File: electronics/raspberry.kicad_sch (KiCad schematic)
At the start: 13 parts, among them J1 Raspberry_Pi_4, J2 TUB00154 Analog Control, U1 LT1009CZ, U2 TLV5618A, U3 SFH900, U4 SFH900, U5 MCP3202, U7 LM4040LP-5

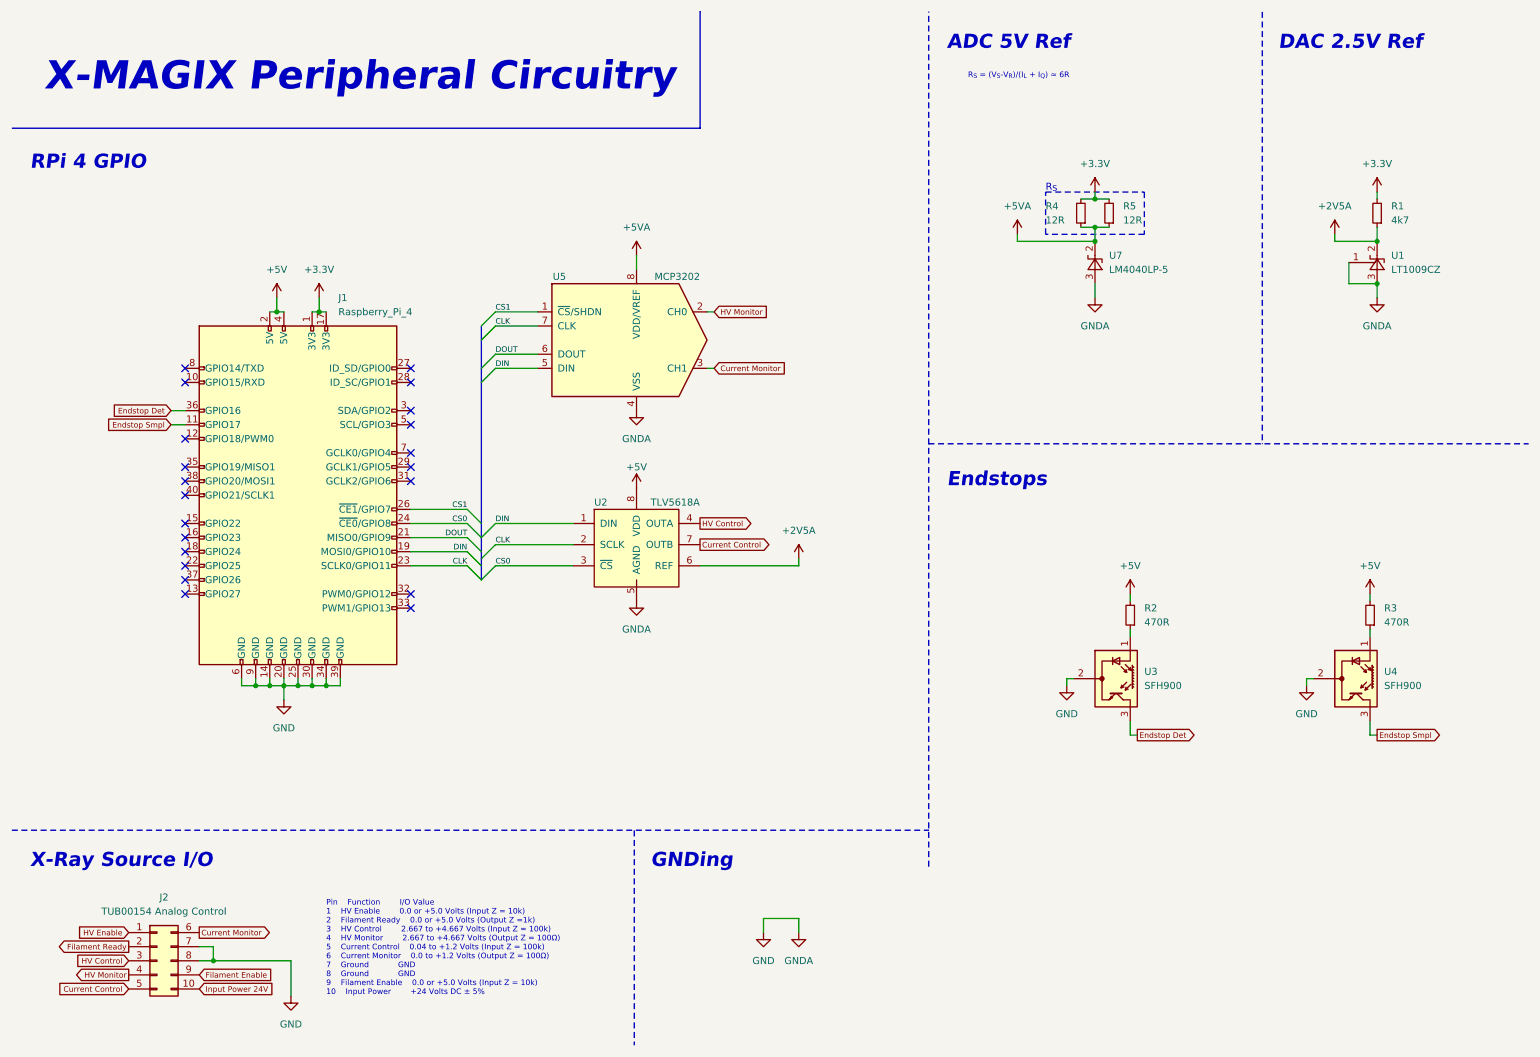
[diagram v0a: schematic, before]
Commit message: Tube Interface Board Docs
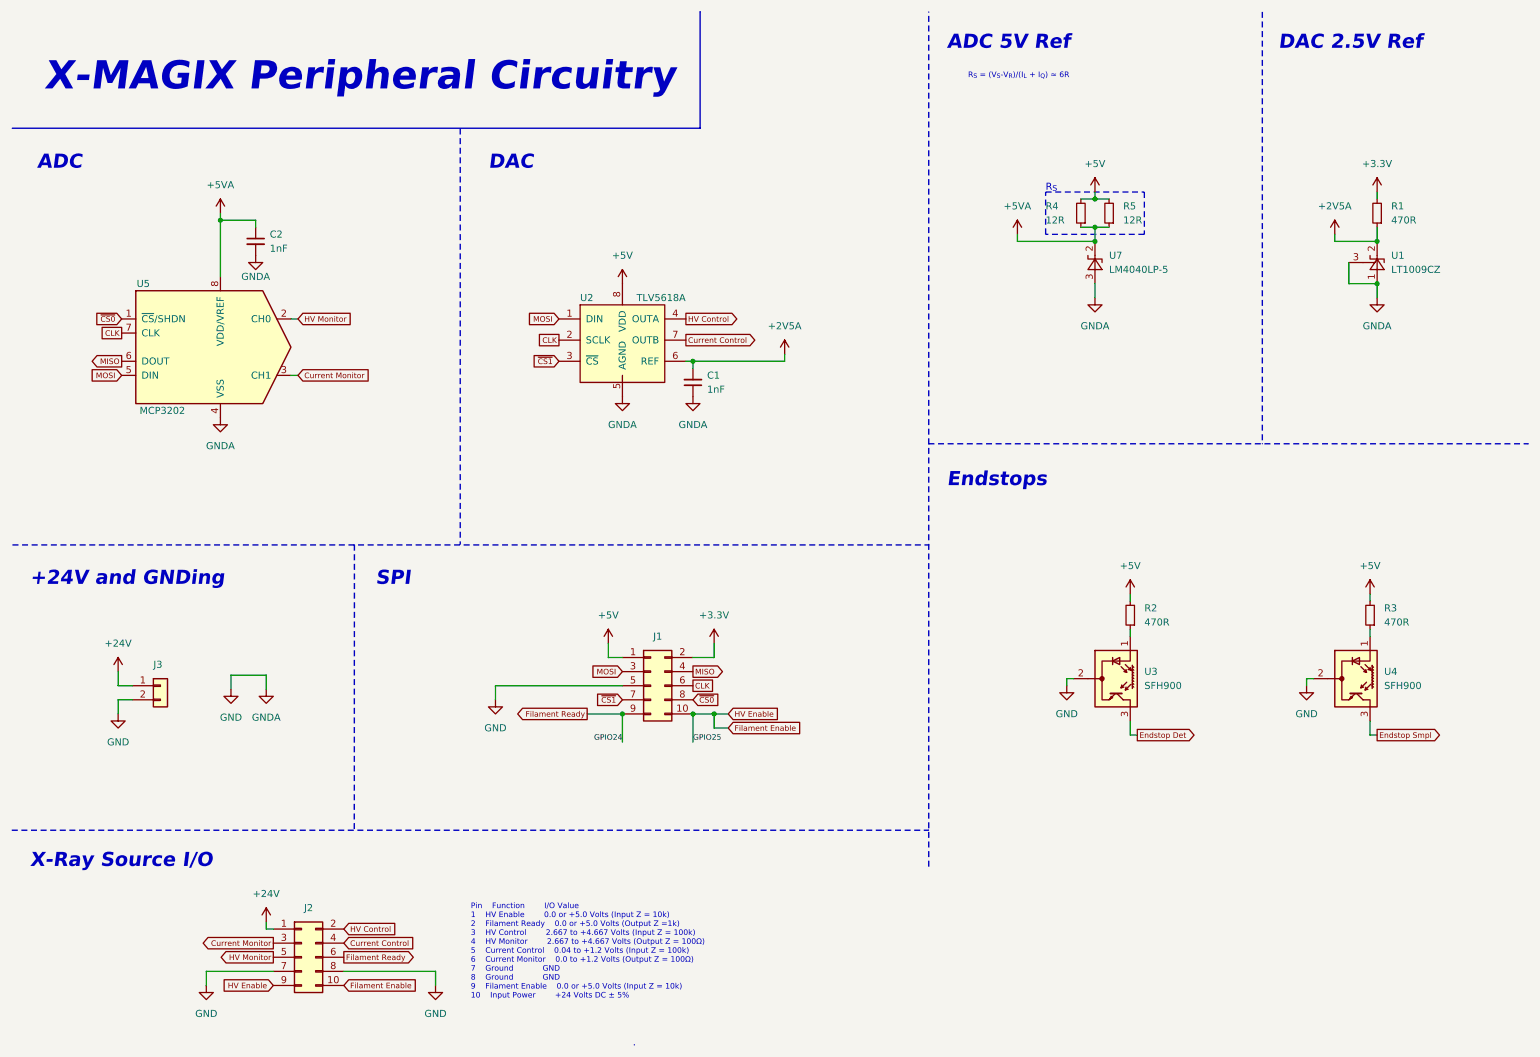
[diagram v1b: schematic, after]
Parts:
- removed J1: Raspberry_Pi_4, symbol Connector:Raspberry_Pi_2_3
- removed J2: TUB00154 Analog Control, symbol Connector_Generic:Conn_02x05_Top_Bottom
- added C1, C2: 1nF, custom_footprints:C_Disc_D3.0mm_W2.0mm_P2.54mm, symbol Device:C_Small
- added J1, J2: Conn_02x05_Counter_Clockwise, Connector_PinHeader_2.54mm:PinHeader_2x05_P2.54mm_Vertical, symbol Connector_Generic:Conn_02x05_Odd_Even
- added J3: Conn_01x02, custom_footprints:JST_XH_B2B-XH-A_1x02_P2.54mm_Vertical, symbol Connector_Generic:Conn_01x02
- R1: value 4k7 -> 470R; footprint (none) -> Resistor_THT:R_Axial_DIN0204_L3.6mm_D1.6mm_P7.62mm_Horizontal
- R4, R5: footprint (none) -> Resistor_THT:R_Axial_DIN0204_L3.6mm_D1.6mm_P7.62mm_Horizontal
- U1, U7: footprint Package_TO_SOT_THT:TO-92_Inline -> custom_footprints:TO-92L_Wide
- U2: footprint Package_SO:SOIC-8_3.9x4.9mm_P1.27mm -> Package_DIP:DIP-8_W7.62mm
- U5: footprint (none) -> Package_DIP:DIP-8_W7.62mm
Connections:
- net +2V5A: now also C1.2
- net +3.3V: now also J1.2 (Pin_2); no longer R4.2, R5.2
- net +5V: now also R4.2, R5.2, J1.1 (Pin_1)
- net +5VA: now also C2.1
- net CLK: now also J1.6 (Pin_6)
- net Current Control: now also J2.4 (Pin_4)
- net Current Monitor: now also J2.3 (Pin_3)
- net Filament Enable: now also J1.10 (Pin_10), J2.10 (Pin_10), J2.9 (Pin_9)
- net Filament Ready: now also J1.9 (Pin_9), J2.6 (Pin_6)
- net GND: now also C1.1, C2.2, J1.5 (Pin_5), J2.7 (Pin_7), J2.8 (Pin_8), J3.2 (Pin_2)
- net HV Control: now also J2.2 (Pin_2)
- net HV Monitor: now also J2.5 (Pin_5)
- net CS0 renamed ~{CS1}
- net ~{CS1}: now also J1.7 (Pin_7)
- net CS1 renamed ~{CS0}
- net ~{CS0}: now also J1.8 (Pin_8)
- net DIN renamed MOSI
- net MOSI: now also J1.3 (Pin_3)
- net DOUT renamed MISO
- net MISO: now also J1.4 (Pin_4)
- new net +24V: J2.1 (Pin_1), J3.1 (Pin_1)
- no-connect marks 21 -> 0
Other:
- note added: "+24V and GNDing"
- note added: "ADC"
- note added: "DAC"
- note added: "SPI"
- note removed: "GNDing"
- note removed: "RPi 4 GPIO"
- moved on the sheet: U2, U5

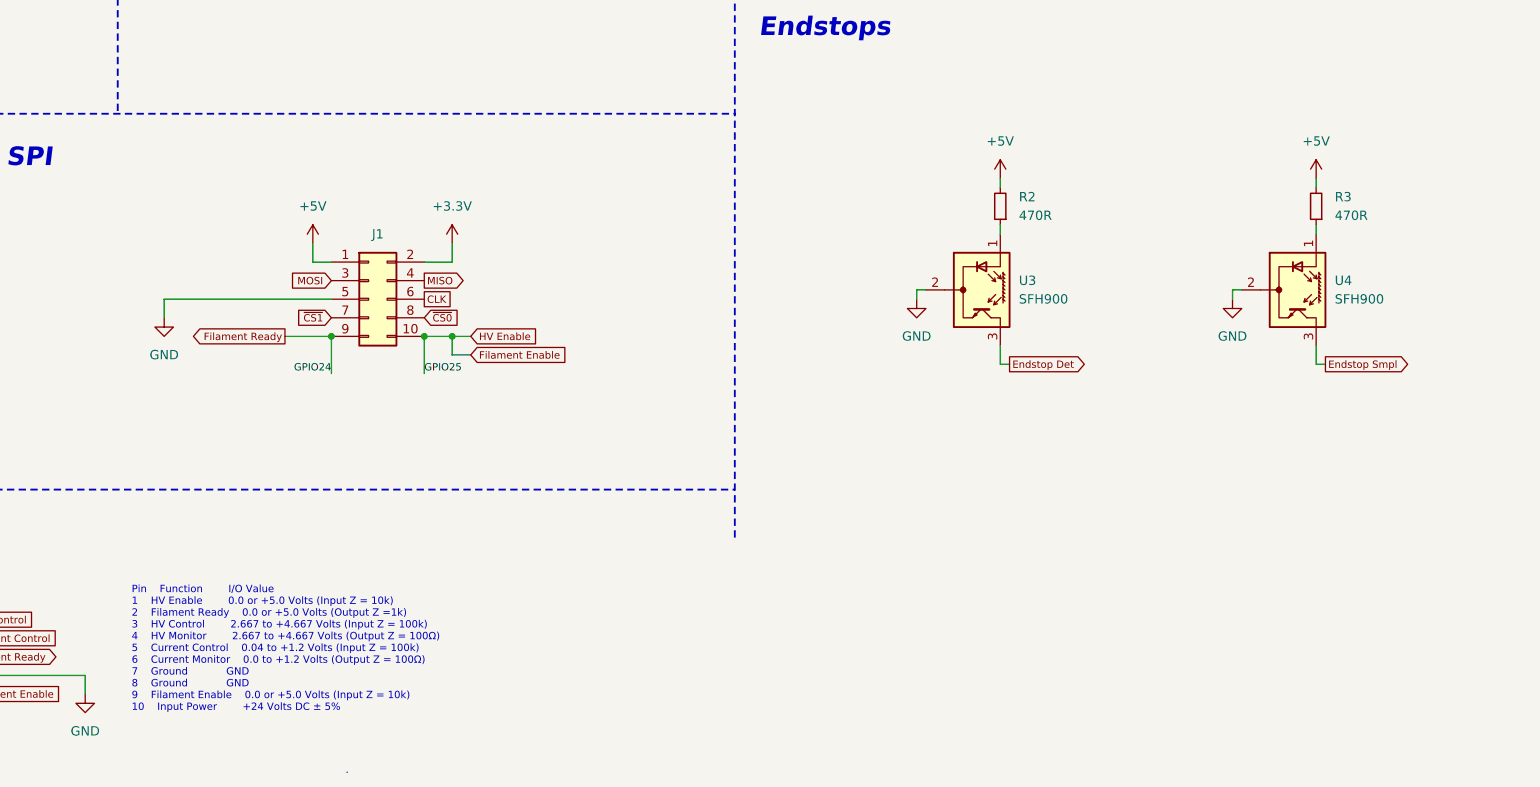
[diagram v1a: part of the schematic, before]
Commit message: endstops optical to tactile
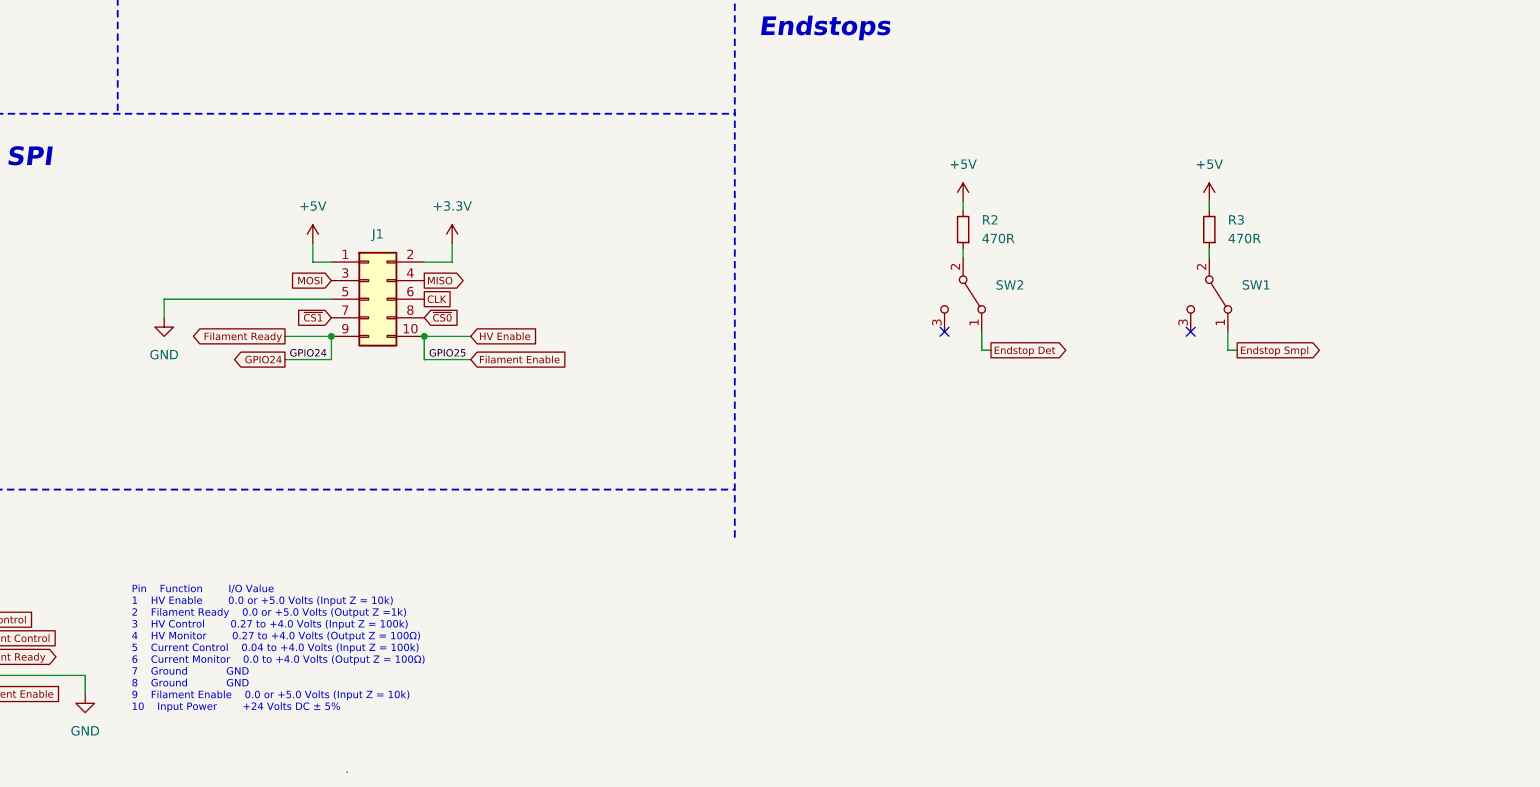
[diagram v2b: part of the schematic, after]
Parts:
- removed U3, U4: SFH900, OptoDevice:Siemens_SFH900, symbol Sensor_Proximity:SFH900
- added SW1, SW2: SW_SPDT, symbol Switch:SW_SPDT
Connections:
- net Endstop Det: now also SW2.1 (A)
- net Endstop Smpl: now also SW1.1 (A)
- net at R2.1: now also SW2.2 (B)
- net at R3.1: now also SW1.2 (B)
- no-connect marks 0 -> 2
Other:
- note added: "Pin Function I/O Value 1 HV Enable 0.0 or +5.0 Volts (Input Z = 10k) 2 Filament Ready 0.0 or +5.0 Volts (Output Z =1k) 3 HV Control 0.27 to +4.0 Volts (Input Z = 100k) 4 HV Monitor 0.27 to +4.0 Volts (Output Z = 100Ω) 5 Current Control 0.04 to +4.0 Volts (Input Z = 100k) 6 Current Monitor 0.0 to +4.0 Volts (Output Z = 100Ω) 7 Ground GND 8 Ground GND 9 Filament Enable 0.0 or +5.0 Volts (Input Z = 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"
- note removed: "Pin Function I/O Value 1 HV Enable 0.0 or +5.0 Volts (Input Z = 10k) 2 Filament Ready 0.0 or +5.0 Volts (Output Z =1k) 3 HV Control 2.667 to +4.667 Volts (Input Z = 100k) 4 HV Monitor 2.667 to +4.667 Volts (Output Z = 100Ω) 5 Current Control 0.04 to +1.2 Volts (Input Z = 100k) 6 Current Monitor 0.0 to +1.2 Volts (Output Z = 100Ω) 7 Ground GND 8 Ground GND 9 Filament Enable 0.0 or +5.0 Volts (Inpu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"
- company: Hochschule RheinMain -> RheinMain University of Applied Sciences
- moved on the sheet: R2, R3

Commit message: schematics bug fix, gitignore
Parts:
- U7: value LM4040LP-5 -> LM4040DIZ-5.0
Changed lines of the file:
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@@
       (effects (font (size 1.27 1.27)) (justify right))
     )
-    (property "Value" "LM4040LP-5" (at 209.55 58.42 90)
+    (property "Value" "LM4040DIZ-5.0" (at 209.55 58.42 90)
       (effects (font (size 1.27 1.27)) (justify right))
     )
